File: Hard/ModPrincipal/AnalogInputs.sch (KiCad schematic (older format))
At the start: 17 parts, among them U201 LM324

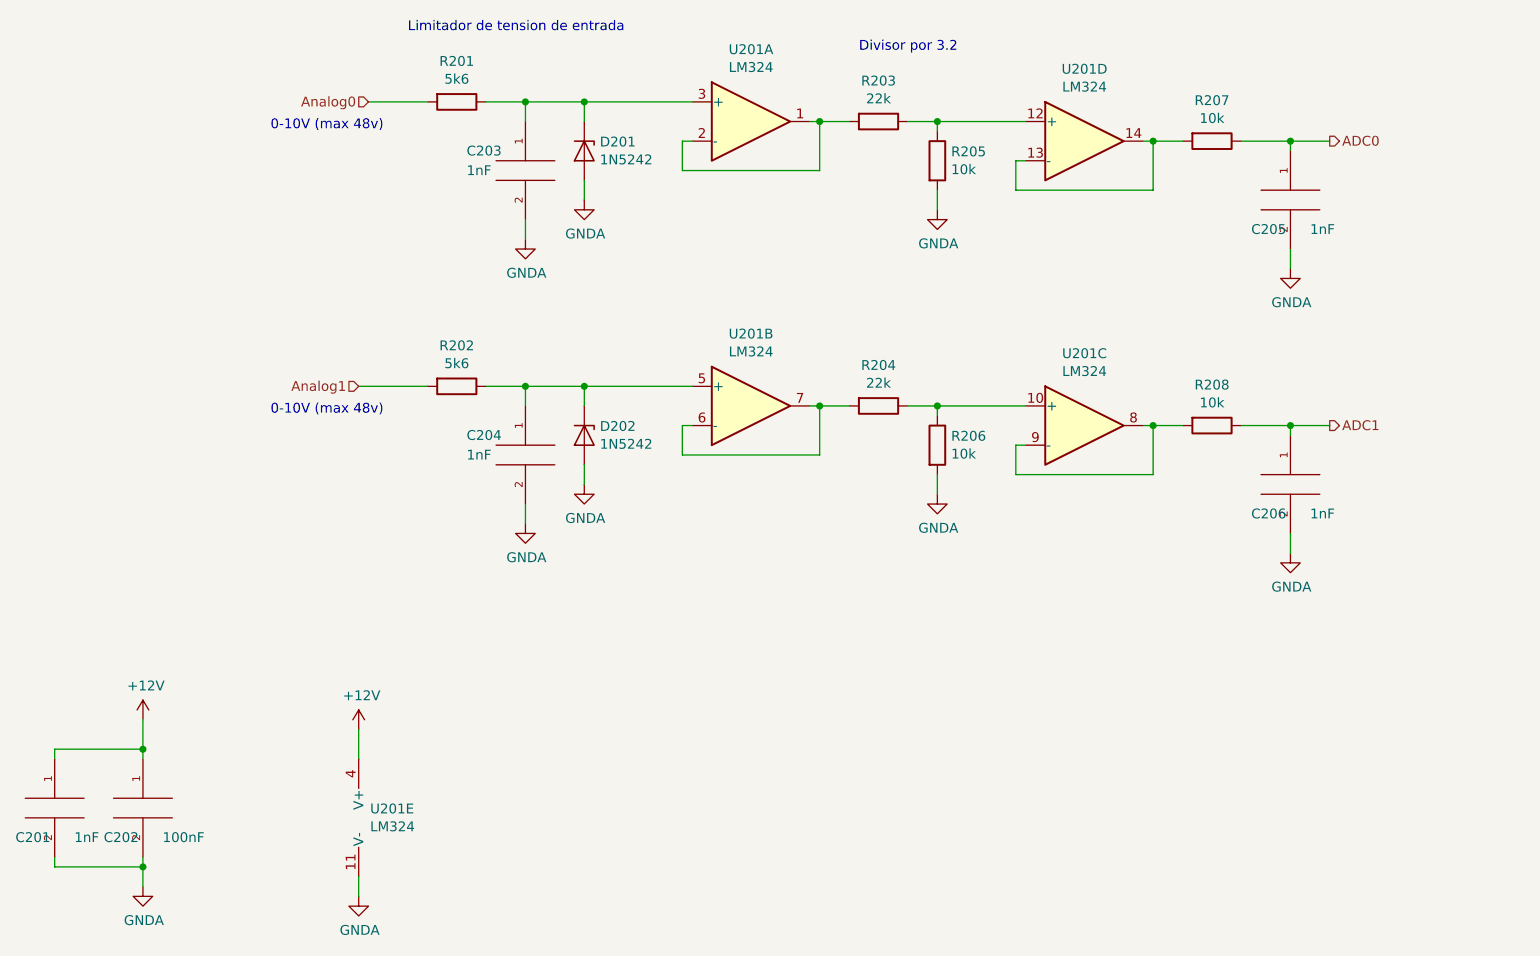
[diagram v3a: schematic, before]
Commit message: Asignación de footprint y corrección de errores de ERC en esquematico
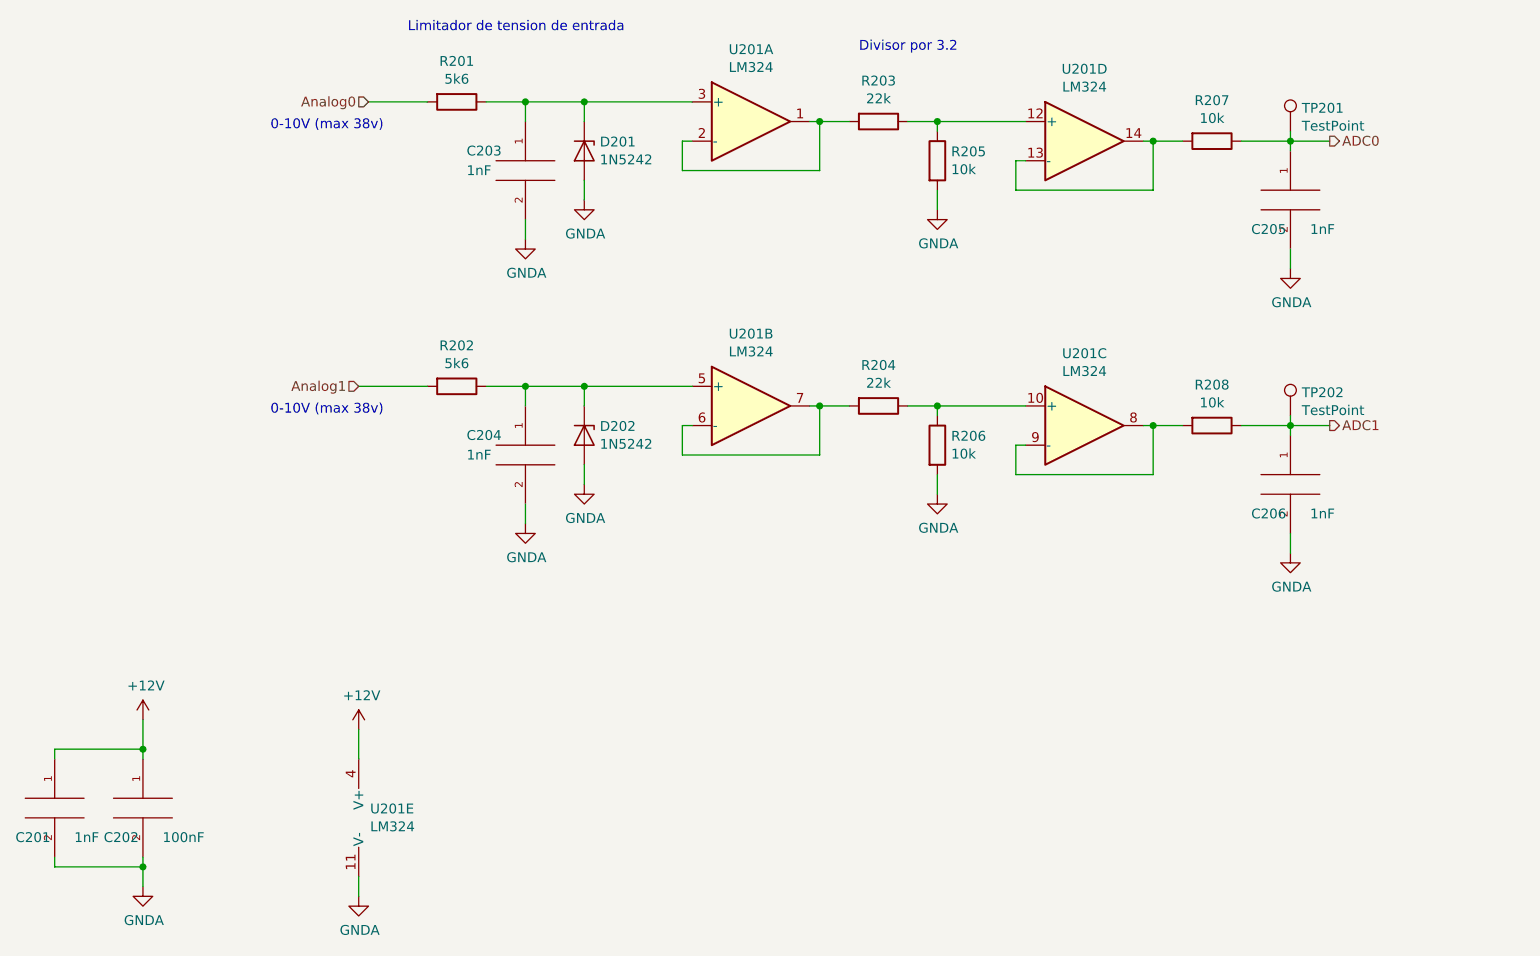
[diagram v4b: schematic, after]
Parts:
- added TP201, TP202: TestPoint, TestPoint:TestPoint_Pad_D1.5mm, symbol Connector:TestPoint
- R201, R202: footprint Resistor_THT:R_Axial_DIN0207_L6.3mm_D2.5mm_P10.16mm_Horizontal -> Resistor_SMD:R_0805_2012Metric_Pad1.15x1.40mm_HandSolder
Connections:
- net ADC0: now also TP201.1
- net ADC1: now also TP202.1
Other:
- note added: "0-10V (max 38v)\n"
- note removed: "0-10V (max 48v)\n"

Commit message: Avance en trazado de pista Modulo principal
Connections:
- net GNDA: no longer C205.2, C206.2
- new net GND: C205.2, C206.2
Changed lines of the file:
@@
-	1    0    0    -1
-$EndComp
-$Comp
-L power:GNDA #PWR0211
-U 1 1 5ECFBDF2
-P 7900 2800
-F 0 "#PWR0211" H 7900 2550 50  0001 C CNN
-F 1 "GNDA" H 7905 2627 50  0000 C CNN
-F 2 "" H 7900 2800 50  0001 C CNN
-F 3 "" H 7900 2800 50  0001 C CNN
-	1    7900 2800
 	1    0    0    -1
 $EndComp
@@
 F 3 "~" H 7900 3900 50  0001 C CNN
 	1    7900 3900
-	1    0    0    -1
-$EndComp
-$Comp
-L power:GNDA #PWR0212
-U 1 1 5ED294B1
-P 7900 4250
-F 0 "#PWR0212" H 7900 4000 50  0001 C CNN
-F 1 "GNDA" H 7905 4077 50  0000 C CNN
-F 2 "" H 7900 4250 50  0001 C CNN
-F 3 "" H 7900 4250 50  0001 C CNN
-	1    7900 4250
 	1    0    0    -1
 $EndComp
@@
 Wire Wire Line
 	4000 4000 4000 4100
+$Comp
+L power:GND #PWR0111
+U 1 1 5EE1B5B1
+P 7900 4250
+F 0 "#PWR0111" H 7900 4000 50  0001 C CNN
+F 1 "GND" H 7905 4077 50  0000 C CNN
+F 2 "" H 7900 4250 50  0001 C CNN
+F 3 "" H 7900 4250 50  0001 C CNN
+	1    7900 4250
+	1    0    0    -1
+$EndComp
+$Comp
+L power:GND #PWR0112
+U 1 1 5EE1DAA9
+P 7900 2800
+F 0 "#PWR0112" H 7900 2550 50  0001 C CNN
+F 1 "GND" H 7905 2627 50  0000 C CNN
+F 2 "" H 7900 2800 50  0001 C CNN
+F 3 "" H 7900 2800 50  0001 C CNN
+	1    7900 2800
+	1    0    0    -1
+$EndComp
 $EndSCHEMATC
